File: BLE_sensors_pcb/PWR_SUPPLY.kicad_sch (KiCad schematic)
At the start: 0 parts

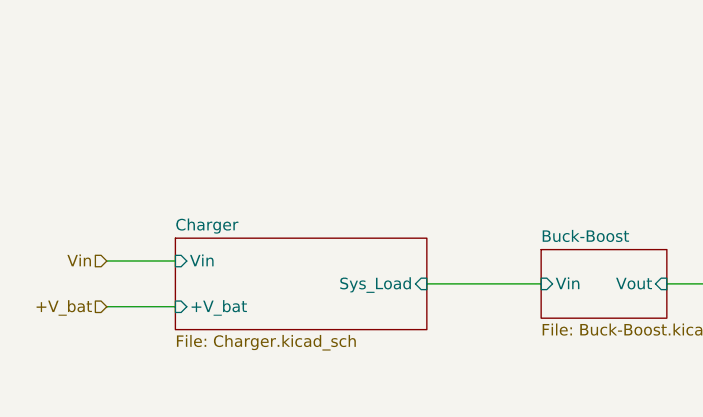
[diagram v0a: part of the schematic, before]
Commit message: Added the usb to serial bridge
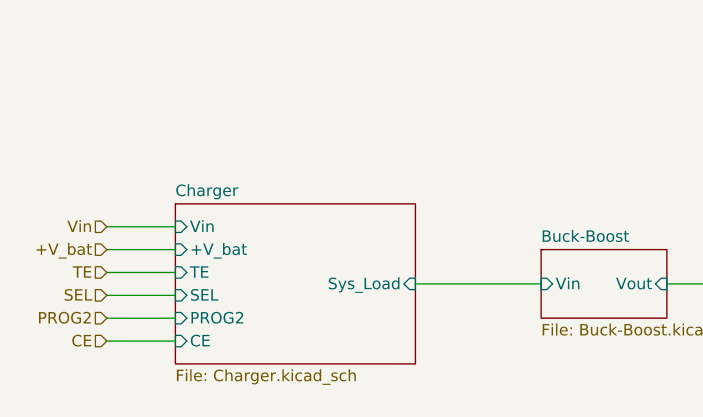
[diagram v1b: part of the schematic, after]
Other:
- sheet Charger ports: added CE, PROG2, SEL, TE; removed none
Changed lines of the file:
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@@
-	(wire
-		(pts
-			(xy 125.73 104.14) (xy 138.43 104.14)
-		)
-		(stroke
-			(width 0)
-			(type default)
-		)
-	)
 	(wire
 		(pts
@@
 	(wire
 		(pts
+			(xy 90.17 107.95) (xy 97.79 107.95)
+		)
+		(stroke
+			(width 0)
+			(type default)
+		)
+	)
+	(wire
+		(pts
 			(xy 167.64 110.49) (xy 167.64 104.14)
 		)
@@
 	(wire
 		(pts
-			(xy 90.17 101.6) (xy 97.79 101.6)
-		)
-		(stroke
-			(width 0)
-			(type default)
-		)
-	)
-	(wire
-		(pts
-			(xy 90.17 106.68) (xy 97.79 106.68)
+			(xy 90.17 97.79) (xy 97.79 97.79)
+		)
+		(stroke
+			(width 0)
+			(type default)
+		)
+	)
+	(wire
+		(pts
+			(xy 124.46 104.14) (xy 138.43 104.14)
 		)
 		(stroke
@@
 	(wire
 		(pts
+			(xy 90.17 110.49) (xy 97.79 110.49)
+		)
+		(stroke
+			(width 0)
+			(type default)
+		)
+	)
+	(wire
+		(pts
+			(xy 90.17 105.41) (xy 97.79 105.41)
+		)
+		(stroke
+			(width 0)
+			(type default)
+		)
+	)
+	(wire
+		(pts
 			(xy 167.64 110.49) (xy 171.45 110.49)
 		)
@@
 	(wire
 		(pts
+			(xy 90.17 100.33) (xy 97.79 100.33)
+		)
+		(stroke
+			(width 0)
+			(type default)
+		)
+	)
+	(wire
+		(pts
 			(xy 190.5 97.79) (xy 167.64 97.79)
 		)
@@
 	(wire
 		(pts
+			(xy 90.17 102.87) (xy 97.79 102.87)
+		)
+		(stroke
+			(width 0)
+			(type default)
+		)
+	)
+	(wire
+		(pts
 			(xy 152.4 104.14) (xy 167.64 104.14)
 		)
@@
 		)
 	)
+	(hierarchical_label "PROG2"
+		(shape input)
+		(at 90.17 107.95 180)
+		(effects
+			(font
+				(size 1.27 1.27)
+			)
+			(justify right)
+		)
+	)
 	(hierarchical_label "+3V3_OUT"
 		(shape input)
@@
 	(hierarchical_label "+V_bat"
 		(shape input)
-		(at 90.17 106.68 180)
+		(at 90.17 100.33 180)
 		(effects
 			(font
@@
 		)
 	)
+	(hierarchical_label "SEL"
+		(shape input)
+		(at 90.17 105.41 180)
+		(effects
+			(font
+				(size 1.27 1.27)
+			)
+			(justify right)
+		)
+	)
+	(hierarchical_label "CE"
+		(shape input)
+		(at 90.17 110.49 180)
+		(effects
+			(font
+				(size 1.27 1.27)
+			)
+			(justify right)
+		)
+	)
+	(hierarchical_label "TE"
+		(shape input)
+		(at 90.17 102.87 180)
+		(effects
+			(font
+				(size 1.27 1.27)
+			)
+			(justify right)
+		)
+	)
 	(hierarchical_label "Vin"
 		(shape input)
-		(at 90.17 101.6 180)
+		(at 90.17 97.79 180)
 		(effects
 			(font
@@
 	)
 	(sheet
-		(at 97.79 99.06)
-		(size 27.94 10.16)
+		(at 97.79 95.25)
+		(size 26.67 17.78)
 		(exclude_from_sim no)
 		(in_bom yes)
@@
 		)
 		(property "Sheetname" "Charger"
-			(at 97.79 98.3484 0)
+			(at 97.79 94.5384 0)
 			(effects
 				(font
@@
 		)
 		(property "Sheetfile" "Charger.kicad_sch"
-			(at 97.79 109.8046 0)
+			(at 97.79 113.6146 0)
 			(effects
 				(font
@@
 		)
 		(pin "+V_bat" input
-			(at 97.79 106.68 180)
+			(at 97.79 100.33 180)
 			(effects
 				(font
@@
 		)
 		(pin "Sys_Load" input
-			(at 125.73 104.14 0)
+			(at 124.46 104.14 0)
 			(effects
 				(font
@@
 		)
 		(pin "Vin" input
-			(at 97.79 101.6 180)
-			(effects
-				(font
+			(at 97.79 97.79 180)
+			(effects
+				(font
+					(size 1.27 1.27)
+				)
+				(justify left)
+			)
+		)
+		(pin "CE" input
+			(at 97.79 110.49 180)
+			(effects
+				(font
+					(size 1.27 1.27)
+				)
+				(justify left)
+			)
+		)
+		(pin "PROG2" input
+			(at 97.79 107.95 180)
+			(effects
+				(font
+					(size 1.27 1.27)
+				)
+				(justify left)
+			)
+		)
+		(pin "SEL" input
+			(at 97.79 105.41 180)
+			(effects
+				(font
+					(size 1.27 1.27)
+				)
+				(justify left)
+			)
+		)
+		(pin "TE" input
+			(at 97.79 102.87 180)
+			(effects
+				(font

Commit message: Initial pcb placement
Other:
- sheet Charger ports: added none; removed CE, PROG2, SEL, TE
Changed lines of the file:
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@@
-	(wire
-		(pts
-			(xy 90.17 107.95) (xy 97.79 107.95)
-		)
-		(stroke
-			(width 0)
-			(type default)
-		)
-	)
 	(wire
 		(pts
@@
 	(wire
 		(pts
-			(xy 90.17 97.79) (xy 97.79 97.79)
-		)
-		(stroke
-			(width 0)
-			(type default)
-		)
-	)
-	(wire
-		(pts
 			(xy 124.46 104.14) (xy 138.43 104.14)
 		)
@@
 	(wire
 		(pts
-			(xy 90.17 110.49) (xy 97.79 110.49)
-		)
-		(stroke
-			(width 0)
-			(type default)
-		)
-	)
-	(wire
-		(pts
-			(xy 90.17 105.41) (xy 97.79 105.41)
+			(xy 91.44 100.33) (xy 100.33 100.33)
 		)
 		(stroke
@@
 	(wire
 		(pts
-			(xy 90.17 100.33) (xy 97.79 100.33)
-		)
-		(stroke
-			(width 0)
-			(type default)
-		)
-	)
-	(wire
-		(pts
 			(xy 190.5 97.79) (xy 167.64 97.79)
 		)
@@
 	(wire
 		(pts
-			(xy 90.17 102.87) (xy 97.79 102.87)
+			(xy 92.71 105.41) (xy 100.33 105.41)
 		)
 		(stroke
@@
 		)
 	)
-	(hierarchical_label "PROG2"
-		(shape input)
-		(at 90.17 107.95 180)
+	(hierarchical_label "+3V3_OUT"
+		(shape input)
+		(at 190.5 97.79 0)
+		(effects
+			(font
+				(size 1.27 1.27)
+			)
+			(justify left)
+		)
+	)
+	(hierarchical_label "+V_bat"
+		(shape input)
+		(at 92.71 105.41 180)
 		(effects
 			(font
@@
 		)
 	)
-	(hierarchical_label "+3V3_OUT"
-		(shape input)
-		(at 190.5 97.79 0)
+	(hierarchical_label "+1V8_OUT"
+		(shape input)
+		(at 190.5 110.49 0)
 		(effects
 			(font
@@
 		)
 	)
-	(hierarchical_label "+V_bat"
-		(shape input)
-		(at 90.17 100.33 180)
-		(effects
-			(font
-				(size 1.27 1.27)
-			)
-			(justify right)
-		)
-	)
-	(hierarchical_label "+1V8_OUT"
-		(shape input)
-		(at 190.5 110.49 0)
-		(effects
-			(font
-				(size 1.27 1.27)
-			)
-			(justify left)
-		)
-	)
-	(hierarchical_label "SEL"
-		(shape input)
-		(at 90.17 105.41 180)
-		(effects
-			(font
-				(size 1.27 1.27)
-			)
-			(justify right)
-		)
-	)
-	(hierarchical_label "CE"
-		(shape input)
-		(at 90.17 110.49 180)
-		(effects
-			(font
-				(size 1.27 1.27)
-			)
-			(justify right)
-		)
-	)
-	(hierarchical_label "TE"
-		(shape input)
-		(at 90.17 102.87 180)
-		(effects
-			(font
-				(size 1.27 1.27)
-			)
-			(justify right)
-		)
-	)
 	(hierarchical_label "Vin"
 		(shape input)
-		(at 90.17 97.79 180)
+		(at 91.44 100.33 180)
 		(effects
 			(font
@@
 	)
 	(sheet
-		(at 97.79 95.25)
-		(size 26.67 17.78)
+		(at 100.33 97.79)
+		(size 24.13 10.16)
 		(exclude_from_sim no)
 		(in_bom yes)
@@
 		)
 		(property "Sheetname" "Charger"
-			(at 97.79 94.5384 0)
+			(at 100.33 97.0784 0)
 			(effects
 				(font
@@
 		)
 		(property "Sheetfile" "Charger.kicad_sch"
-			(at 97.79 113.6146 0)
+			(at 100.33 108.5346 0)
 			(effects
 				(font
@@
 		)
 		(pin "+V_bat" input
-			(at 97.79 100.33 180)
+			(at 100.33 105.41 180)
 			(effects
 				(font
@@
 		)
 		(pin "Vin" input
-			(at 97.79 97.79 180)
-			(effects
-				(font
-					(size 1.27 1.27)
-				)
-				(justify left)
-			)
-		)
-		(pin "CE" input
-			(at 97.79 110.49 180)
-			(effects
-				(font
-					(size 1.27 1.27)
-				)
-				(justify left)
-			)
-		)
-		(pin "PROG2" input
-			(at 97.79 107.95 180)
-			(effects
-				(font
-					(size 1.27 1.27)
-				)
-				(justify left)
-			)
-		)
-		(pin "SEL" input
-			(at 97.79 105.41 180)
-			(effects
-				(font
-					(size 1.27 1.27)
-				)
-				(justify left)
-			)
-		)
-		(pin "TE" input
-			(at 97.79 102.87 180)
-			(effects
-				(font
+			(at 100.33 100.33 180)
+			(effects
+				(font

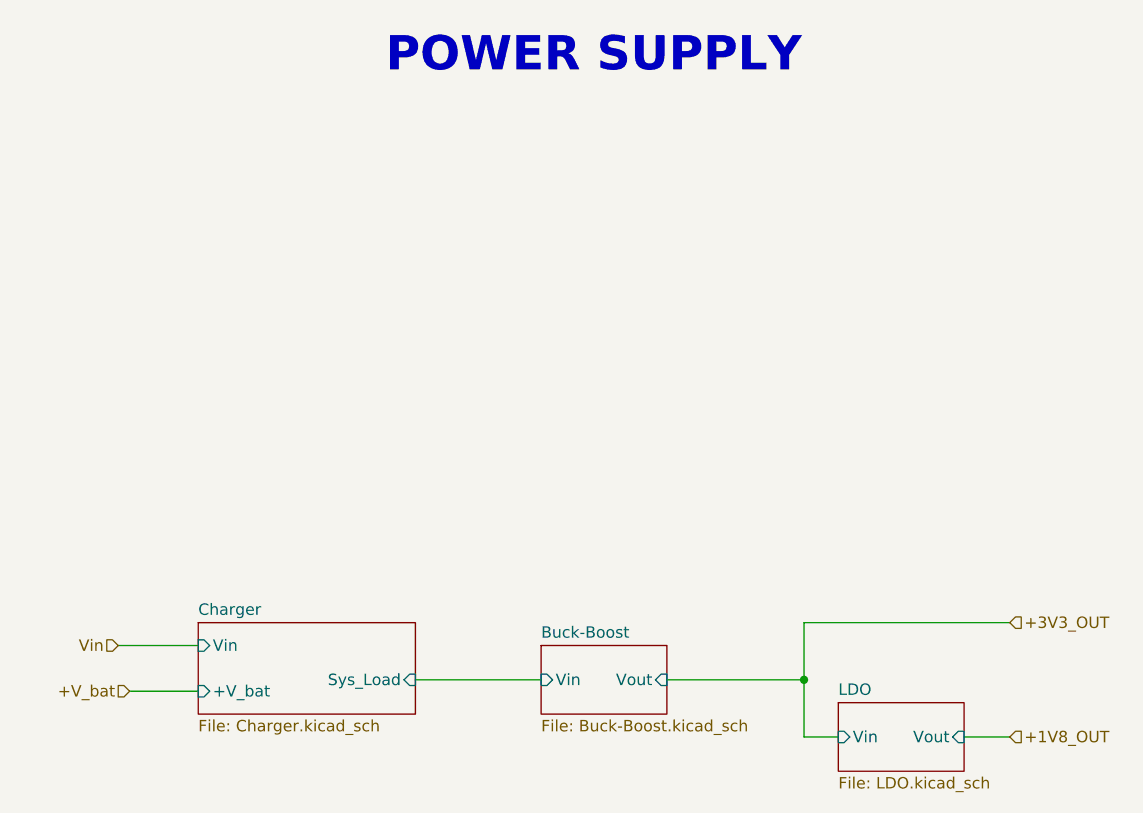
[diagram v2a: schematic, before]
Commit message: Changed bme power supply and added pull up to tag connect
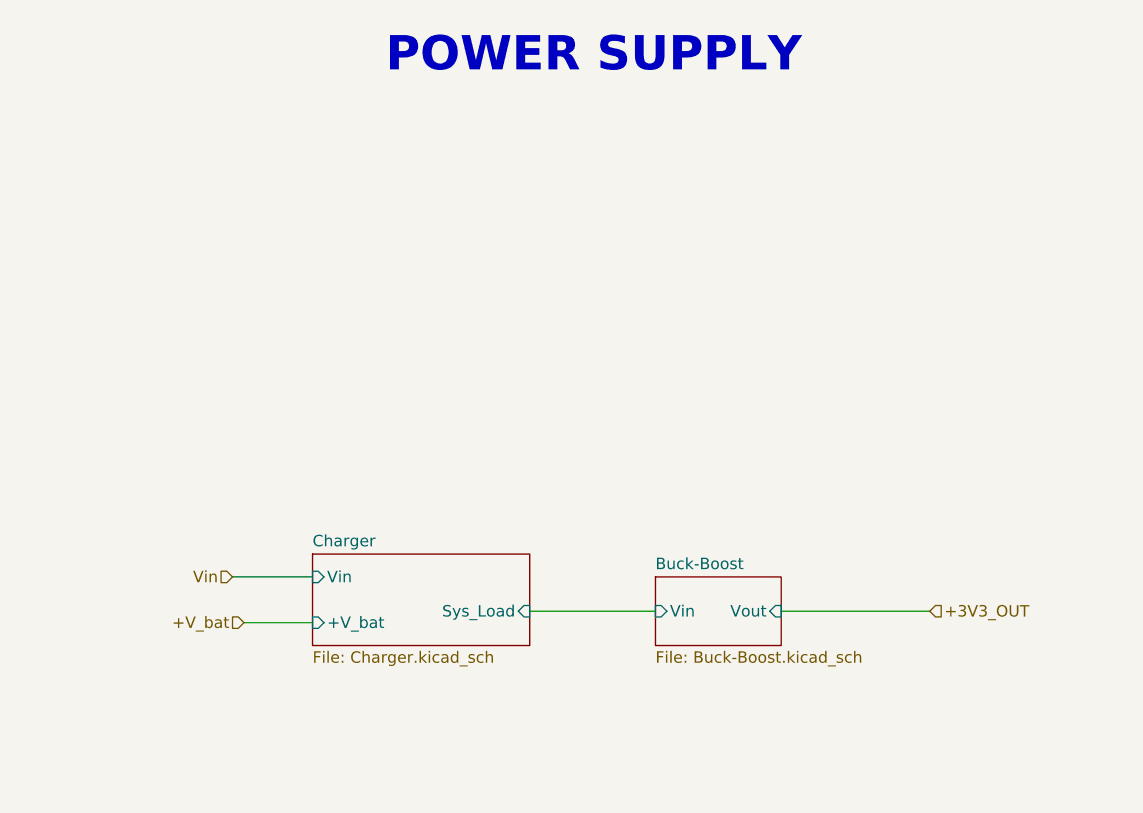
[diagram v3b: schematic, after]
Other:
- removed sheet LDO
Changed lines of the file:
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@@
 		)
-	)
-	(junction
-		(at 167.64 104.14)
-		(diameter 0)
-		(color 0 0 0 0)
 	)
 	(wire
 		(pts
-			(xy 185.42 110.49) (xy 190.5 110.49)
+			(xy 137.16 96.52) (xy 151.13 96.52)
 		)
 		(stroke
@@
 	(wire
 		(pts
-			(xy 167.64 110.49) (xy 167.64 104.14)
+			(xy 104.14 92.71) (xy 113.03 92.71)
 		)
 		(stroke
@@
 	(wire
 		(pts
-			(xy 124.46 104.14) (xy 138.43 104.14)
+			(xy 105.41 97.79) (xy 113.03 97.79)
 		)
 		(stroke
@@
 	(wire
 		(pts
-			(xy 167.64 97.79) (xy 167.64 104.14)
-		)
-		(stroke
-			(width 0)
-			(type default)
-		)
-	)
-	(wire
-		(pts
-			(xy 91.44 100.33) (xy 100.33 100.33)
-		)
-		(stroke
-			(width 0)
-			(type default)
-		)
-	)
-	(wire
-		(pts
-			(xy 167.64 110.49) (xy 171.45 110.49)
-		)
-		(stroke
-			(width 0)
-			(type default)
-		)
-	)
-	(wire
-		(pts
-			(xy 190.5 97.79) (xy 167.64 97.79)
-		)
-		(stroke
-			(width 0)
-			(type default)
-		)
-	)
-	(wire
-		(pts
-			(xy 92.71 105.41) (xy 100.33 105.41)
-		)
-		(stroke
-			(width 0)
-			(type default)
-		)
-	)
-	(wire
-		(pts
-			(xy 152.4 104.14) (xy 167.64 104.14)
+			(xy 165.1 96.52) (xy 181.61 96.52)
 		)
 		(stroke
@@
 	(hierarchical_label "+3V3_OUT"
 		(shape input)
-		(at 190.5 97.79 0)
+		(at 181.61 96.52 0)
 		(effects
 			(font
@@
 	(hierarchical_label "+V_bat"
 		(shape input)
-		(at 92.71 105.41 180)
+		(at 105.41 97.79 180)
 		(effects
 			(font
@@
 		)
 	)
-	(hierarchical_label "+1V8_OUT"
-		(shape input)
-		(at 190.5 110.49 0)
-		(effects
-			(font
-				(size 1.27 1.27)
-			)
-			(justify left)
-		)
-	)
 	(hierarchical_label "Vin"
 		(shape input)
-		(at 91.44 100.33 180)
+		(at 104.14 92.71 180)
 		(effects
 			(font
@@
 	)
 	(sheet
-		(at 138.43 100.33)
+		(at 151.13 92.71)
 		(size 13.97 7.62)
 		(exclude_from_sim no)
@@
 		)
 		(property "Sheetname" "Buck-Boost"
-			(at 138.43 99.6184 0)
+			(at 151.13 91.9984 0)
 			(effects
 				(font
@@
 		)
 		(property "Sheetfile" "Buck-Boost.kicad_sch"
-			(at 138.43 108.5346 0)
+			(at 151.13 100.9146 0)
 			(effects
 				(font
@@
 		)
 		(pin "Vin" input
-			(at 138.43 104.14 180)
+			(at 151.13 96.52 180)
 			(effects
 				(font
@@
 		)
 		(pin "Vout" input
-			(at 152.4 104.14 0)
+			(at 165.1 96.52 0)
 			(effects
 				(font
@@
 	)
 	(sheet
-		(at 100.33 97.79)
+		(at 113.03 90.17)
 		(size 24.13 10.16)
 		(exclude_from_sim no)
@@
 		)
 		(property "Sheetname" "Charger"
-			(at 100.33 97.0784 0)
+			(at 113.03 89.4584 0)
 			(effects
 				(font
@@
 		)
 		(property "Sheetfile" "Charger.kicad_sch"
-			(at 100.33 108.5346 0)
+			(at 113.03 100.9146 0)
 			(effects
 				(font
@@
 		)
 		(pin "+V_bat" input
-			(at 100.33 105.41 180)
+			(at 113.03 97.79 180)
 			(effects
 				(font
@@
 		)
 		(pin "Sys_Load" input
-			(at 124.46 104.14 0)
+			(at 137.16 96.52 0)
 			(effects
 				(font
@@
 		)
 		(pin "Vin" input
-			(at 100.33 100.33 180)
+			(at 113.03 92.71 180)
 			(effects
 				(font
@@
 				)
 			)
-		)
-	)
-	(sheet
-		(at 171.45 106.68)
-		(size 13.97 7.62)
-		(exclude_from_sim no)
-		(in_bom yes)
-		(on_board yes)
-		(dnp no)
-		(fields_autoplaced yes)
-		(stroke
-			(width 0.1524)
-			(type solid)
-		)
-		(fill
-			(color 255 255 194 1.0000)
-		)
-		(property "Sheetname" "LDO"
-			(at 171.45 105.9684 0)
-			(effects
-				(font
-					(size 1.27 1.27)
-				)
-				(justify left bottom)
-			)
-		)
-		(property "Sheetfile" "LDO.kicad_sch"
-			(at 171.45 114.8846 0)
-			(effects
-				(font
-					(size 1.27 1.27)
-				)
-				(justify left top)
-			)
-		)
-		(pin "Vin" input
-			(at 171.45 110.49 180)
-			(effects
-				(font
-					(size 1.27 1.27)
-				)
-				(justify left)
-			)
-		)
-		(pin "Vout" input
-			(at 185.42 110.49 0)
-			(effects
-				(font
-					(size 1.27 1.27)
-				)
-				(justify right)
-			)
-		)
-		(instances
-			(project "BLE_sensors"
-				(path "/06b47d3c-6b7b-411b-8755-cae193722202/30528618-a979-4bf1-b774-eef2b8cf727d"
-					(page "5")
-				)
-			)
